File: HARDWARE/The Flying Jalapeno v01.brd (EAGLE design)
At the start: 73.7 x 52.1 mm, 79 parts, among them J1 ., J2 7V, Q1 8/16MHz, Q2 NPN, Q3 P-Channel MOSFET, Q4 NPN, Q5 P-Channel MOSFET, U1 ATMEGA328

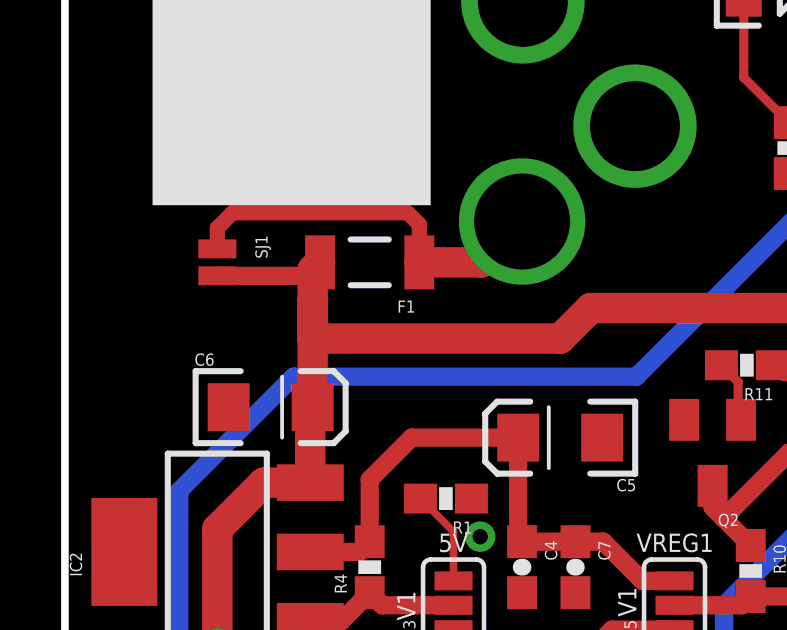
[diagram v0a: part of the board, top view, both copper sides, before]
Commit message: Power input Diode
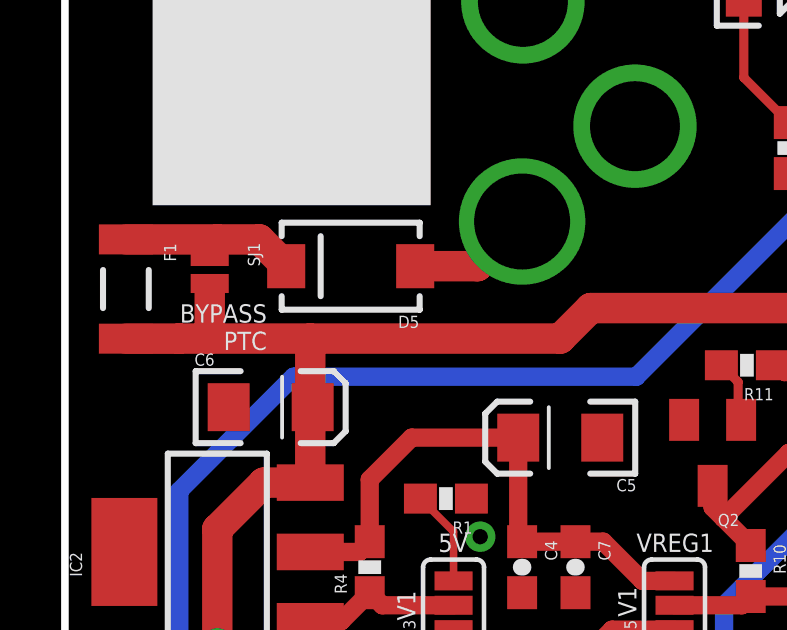
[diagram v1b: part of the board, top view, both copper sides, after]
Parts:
- added D5: MBRA140, SparkFun-DiscreteSemi:SMA-DIODE
- moved F1 8.18 mm to (2.03, 38.5), turned to 270 degrees
- moved SJ1 0.36 mm to (4.83, 39.1)
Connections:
- new net N$24: D5.A, J2.PWR
- net N$15: now also D5.C; no longer J2.PWR
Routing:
- net N$15: track 13.1 -> 6.39 mm
- net N$24: track 0.00 -> 4.18 mm
- net RAW: track 119.7 -> 120.6 mm
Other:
- board text added: "BYPASS PTC"
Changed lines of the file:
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@@
 <?xml version="1.0" encoding="utf-8"?>
 <!DOCTYPE eagle SYSTEM "eagle.dtd">
-<eagle version="6.5.0">
+<eagle version="7.2.0">
 <drawing>
 <settings>
@@
 <layer number="47" name="Measures" color="7" fill="1" visible="no" active="yes"/>
 <layer number="48" name="Document" color="7" fill="1" visible="no" active="yes"/>
-<layer number="49" name="Reference" color="13" fill="1" visible="yes" active="yes"/>
+<layer number="49" name="Reference" color="13" fill="1" visible="no" active="yes"/>
 <layer number="50" name="dxf" color="7" fill="1" visible="no" active="yes"/>
 <layer number="51" name="tDocu" color="6" fill="1" visible="yes" active="yes"/>
@@
 <text x="67.945" y="48.387" size="1.27" layer="21" font="vector" ratio="15">FTDI</text>
 <text x="66.675" y="47.117" size="1.016" layer="21" font="vector" ratio="15">VOLTAGE</text>
+<text x="6.731" y="37.973" size="0.6096" layer="21" font="vector" ratio="15" rot="R180">BYPASS
+ PTC</text>
 </plain>
 <attributes>
@@
 <pass name="Default">
 <param name="RoutingGrid" value="5mil"/>
+<param name="AutoGrid" value="1"/>
+<param name="Efforts" value="0"/>
+<param name="TopRouterVariant" value="1"/>
 <param name="tpViaShape" value="round"/>
 <param name="PrefDir.1" value="-"/>
@@
 <element name="C8" library="SparkFun-Capacitors" package="CPOL-RADIAL-100UF-25V" value="100uF" x="31.75" y="17.78" rot="MR270"/>
 <element name="FRAME1" library="SparkFun-Aesthetics" package="CREATIVE_COMMONS" value="FRAME-LEDGER" x="-1.27" y="-12.7"/>
-<element name="F1" library="Testing" package="PTC-1206-WIDE" value="" x="10.16" y="39.37" rot="R180"/>
+<element name="F1" library="Testing" package="PTC-1206-WIDE" value="" x="2.032" y="38.481" rot="R270"/>
 <element name="J2" library="SparkFun" package="POWER_JACK_PTH_LOCK" value="7V" x="15.24" y="54.61" rot="MR180"/>
-<element name="SJ1" library="SparkFun-Passives" package="PAD-JUMPER-2-NO_NO_SILK" value="PTC Bypass" x="5.08" y="39.37" rot="R270"/>
+<element name="SJ1" library="SparkFun-Passives" package="PAD-JUMPER-2-NO_NO_SILK" value="PTC Bypass" x="4.826" y="39.116" rot="R270"/>
 <element name="C9" library="SparkFun" package="0603-CAP" value="0.1uF" x="59.69" y="33.02" rot="R90"/>
 <element name="C10" library="SparkFun" package="EIA3216" value="10uF" x="43.18" y="46.99" rot="R180"/>
@@
 <element name="LOGO3" library="SparkFun-Aesthetics" package="SFE_LOGO_FLAME_.1" value="SFE_LOGO_FLAME.1_INCH" x="45.72" y="41.021"/>
 <element name="LOGO4" library="SparkFun-Aesthetics" package="OSHW-LOGO-L" value="OSHW-LOGOL" x="8.89" y="6.35" rot="MR0"/>
+<element name="D5" library="SparkFun-DiscreteSemi" package="SMA-DIODE" value="MBRA140" x="9.525" y="39.243" rot="R180">
+<attribute name="PROD_ID" value="DIO-08053" x="9.525" y="39.243" size="1.778" layer="27" font="vector" ratio="15" rot="R180" display="off"/>
+</element>
 </elements>
 <signals>
@@
 <contactref element="SJ6" pad="1"/>
 <contactref element="JP4" pad="4"/>
-<wire x1="8.506" y1="39.37" x2="8.258" y2="39.122" width="1.016" layer="1"/>
-<wire x1="8.258" y1="39.122" x2="8.258" y2="38.1" width="1.016" layer="1"/>
-<wire x1="8.258" y1="37.846" x2="8.258" y2="34.544" width="1.016" layer="1"/>
 <wire x1="8.258" y1="34.544" x2="8.1788" y2="34.4648" width="1.016" layer="1"/>
 <wire x1="8.1788" y1="34.4648" x2="8.1788" y2="32.0294" width="1.016" layer="1"/>
@@
 <wire x1="7.75" y1="22.225" x2="7.75" y2="19.8852" width="1.016" layer="1"/>
 <wire x1="7.75" y1="19.8852" x2="8.0518" y2="19.5834" width="1.016" layer="1"/>
-<wire x1="5.08" y1="38.92" x2="8.056" y2="38.92" width="0.6096" layer="1"/>
-<wire x1="8.056" y1="38.92" x2="8.506" y2="39.37" width="0.6096" layer="1"/>
 <wire x1="20.32" y1="27.1272" x2="18.2372" y2="27.1272" width="0.6096" layer="1"/>
 <wire x1="18.2372" y1="27.1272" x2="15.24" y2="24.13" width="0.6096" layer="1"/>
@@
 <wire x1="33.5788" y1="46.7614" x2="31.0134" y2="46.7614" width="1.016" layer="1"/>
 <wire x1="29.591" y1="45.339" x2="29.591" y2="40.132" width="1.016" layer="1"/>
-<wire x1="8.258" y1="37.846" x2="8.258" y2="38.1" width="1.016" layer="1"/>
 <wire x1="33.5788" y1="46.7614" x2="33.5788" y2="49.1012" width="1.016" layer="1"/>
 <wire x1="33.5788" y1="49.1012" x2="33.404" y2="49.276" width="1.016" layer="1"/>
@@
 <wire x1="17.78" y1="13.081" x2="17.78" y2="11.43" width="0.6096" layer="1"/>
 <via x="17.78" y="11.43" extent="1-16" drill="0.508"/>
-<wire x1="8.258" y1="37.846" x2="8.255" y2="36.83" width="1.016" layer="1"/>
-<wire x1="8.255" y1="36.83" x2="16.51" y2="36.83" width="1.016" layer="1"/>
 <wire x1="16.51" y1="36.83" x2="17.526" y2="37.846" width="1.016" layer="1"/>
 <wire x1="17.526" y1="37.846" x2="27.305" y2="37.846" width="1.016" layer="1"/>
 <wire x1="27.305" y1="37.846" x2="29.591" y2="40.132" width="1.016" layer="1"/>
 <wire x1="29.591" y1="45.339" x2="31.0134" y2="46.7614" width="1.016" layer="1"/>
+<wire x1="16.51" y1="36.83" x2="8.1788" y2="36.83" width="1.016" layer="1"/>
+<wire x1="8.1788" y1="36.83" x2="4.826" y2="36.83" width="1.016" layer="1"/>
+<wire x1="4.826" y1="36.83" x2="3.81" y2="36.83" width="1.016" layer="1"/>
+<wire x1="2.032" y1="36.827" x2="3.807" y2="36.827" width="1.016" layer="1"/>
+<wire x1="3.807" y1="36.827" x2="3.81" y2="36.83" width="1.016" layer="1"/>
+<wire x1="8.1788" y1="34.4648" x2="8.1788" y2="36.83" width="1.016" layer="1"/>
+<wire x1="4.826" y1="36.83" x2="4.826" y2="38.354" width="1.016" layer="1"/>
+<wire x1="4.826" y1="38.354" x2="4.826" y2="38.666" width="0.254" layer="1"/>
 </signal>
 <signal name="D9">
@@
 <signal name="N$15">
 <contactref element="F1" pad="1"/>
-<contactref element="J2" pad="PWR"/>
 <contactref element="SJ1" pad="1"/>
-<wire x1="15.24" y1="40.7322" x2="13.8778" y2="39.37" width="1.016" layer="1"/>
-<wire x1="13.8778" y1="39.37" x2="11.814" y2="39.37" width="1.016" layer="1"/>
-<wire x1="11.814" y1="39.37" x2="11.814" y2="40.637" width="0.508" layer="1"/>
-<wire x1="5.08" y1="39.82" x2="5.08" y2="40.513" width="0.508" layer="1"/>
-<wire x1="5.08" y1="40.513" x2="5.588" y2="41.021" width="0.508" layer="1"/>
-<wire x1="5.588" y1="41.021" x2="11.43" y2="41.021" width="0.508" layer="1"/>
-<wire x1="11.43" y1="41.021" x2="11.814" y2="40.637" width="0.508" layer="1"/>
+<contactref element="D5" pad="C"/>
+<wire x1="7.375" y1="39.243" x2="6.483" y2="40.135" width="1.016" layer="1"/>
+<wire x1="6.483" y1="40.135" x2="5.08" y2="40.135" width="1.016" layer="1"/>
+<wire x1="5.08" y1="40.135" x2="2.032" y2="40.135" width="1.016" layer="1"/>
+<wire x1="4.826" y1="39.566" x2="5.08" y2="39.82" width="0.254" layer="1"/>
+<wire x1="5.08" y1="39.82" x2="5.08" y2="40.135" width="0.254" layer="1"/>
 </signal>
 <signal name="N$3">
@@
 <wire x1="54.1061625" y1="20.32" x2="54.154421875" y2="20.368259375" width="0.254" layer="1"/>
 </signal>
+<signal name="N$24">
+<contactref element="J2" pad="PWR"/>
+<contactref element="D5" pad="A"/>
+<wire x1="15.24" y1="40.7322" x2="13.7508" y2="39.243" width="1.016" layer="1"/>
+<wire x1="13.7508" y1="39.243" x2="11.675" y2="39.243" width="1.016" layer="1"/>
+</signal>
 </signals>
 <errors>
@@
 </board>
 </drawing>
+<compatibility>
+<note version="6.3" minversion="6.2.2" severity="warning">
+Since Version 6.2.2 text objects can contain more than one line,
+which will not be processed correctly with this version.
+</note>
+</compatibility>
 </eagle>

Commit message: Some PROD_IDS and moved to 100uF SMD caps
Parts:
- C10, C11, C14, C15, C5, C6: device SparkFun:EIA3216 -> SparkFun-Capacitors:EIA3216
- C12, C13, C16, C17, C18, C4, C7, C9: device SparkFun:0603-CAP -> SparkFun-Capacitors:0603-CAP
- C3, C8: device SparkFun-Capacitors:CPOL-RADIAL-100UF-25V -> SparkFun-Capacitors:NIC_10X10.5_CAP
- J2: device SparkFun:POWER_JACK_PTH_LOCK -> SparkFun-Connectors:POWER_JACK_PTH_LOCK
- JP1: device SparkFun:1X06-SMD -> SparkFun-Connectors:1X06-SMD
- moved D4 8.15 mm to (31.1, 20.7), turned to 270 degrees
- moved D1 7.45 mm to (31.2, 26.3), turned to 270 degrees
- moved C8 6.48 mm to (38.1, 16.5), flipped to the top, turned to 180 degrees
- moved C3 6.35 mm to (38.1, 30.5), flipped to the top, turned to 180 degrees
- moved R9 6.21 mm to (46.0, 35.8)
- moved R3 5.33 mm to (46.0, 34.3)
- moved R5 4.91 mm to (31.5, 35.3)
- moved R29 4.88 mm to (44.5, 23.0), turned to 180 degrees
- moved R13 3.78 mm to (46.5, 30.6)
- moved R20 2.47 mm to (36.4, 23.0), turned to 0 degrees
- moved R28 1.42 mm to (40.9, 23.0)
- moved R30 1.27 mm to (44.7, 20.7)
- moved R23 0.90 mm to (40.0, 9.78), turned to 0 degrees
- moved R24 0.63 mm to (45.1, 10.4)
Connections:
- net GND: now also C3.-, C8.-; no longer C3.2, C8.2
- net N$22: now also C3.+; no longer C3.1
- net N$23: now also C8.+; no longer C8.1
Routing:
- net V1: track 47.6 -> 56.3 mm
- net N$5: track 3.69 -> 9.51 mm, vias 0 -> 2
- net A7/PRETESTREAD_V2: track 62.1 -> 65.7 mm
- net A6/PRETESTREAD_V1: track 53.7 -> 50.7 mm
- net N$22: track 12.2 -> 14.6 mm
- net V2: track 33.0 -> 35.2 mm
- net PT-FAIL: track 8.73 -> 6.84 mm
- net N$23: track 12.3 -> 14.2 mm
- net N$11: track 3.49 -> 4.81 mm
- net D5: track 37.4 -> 36.2 mm
- net D12/PRETEST-WRITE: track 81.8 -> 80.8 mm
- net RX: track 66.4 -> 65.4 mm
- net TX: track 58.0 -> 57.3 mm

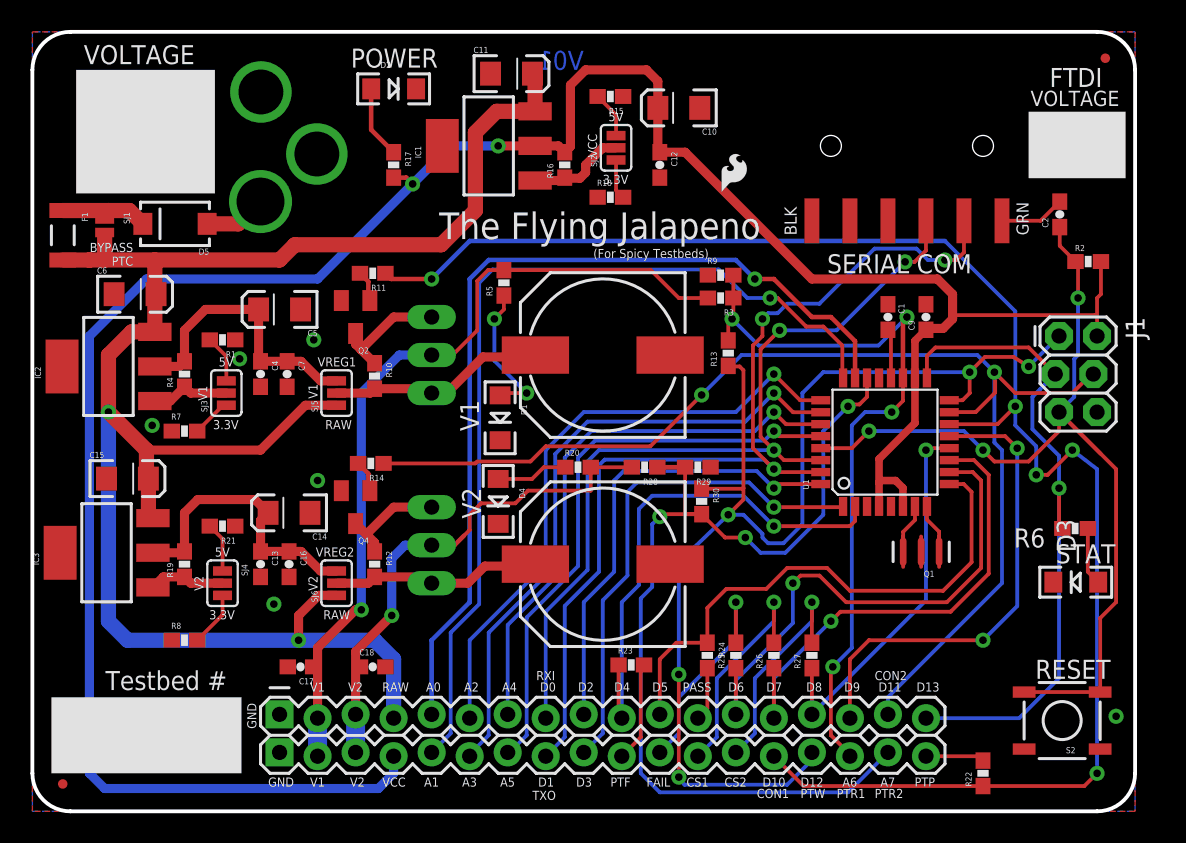
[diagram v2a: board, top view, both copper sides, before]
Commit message: more PROD_IDs
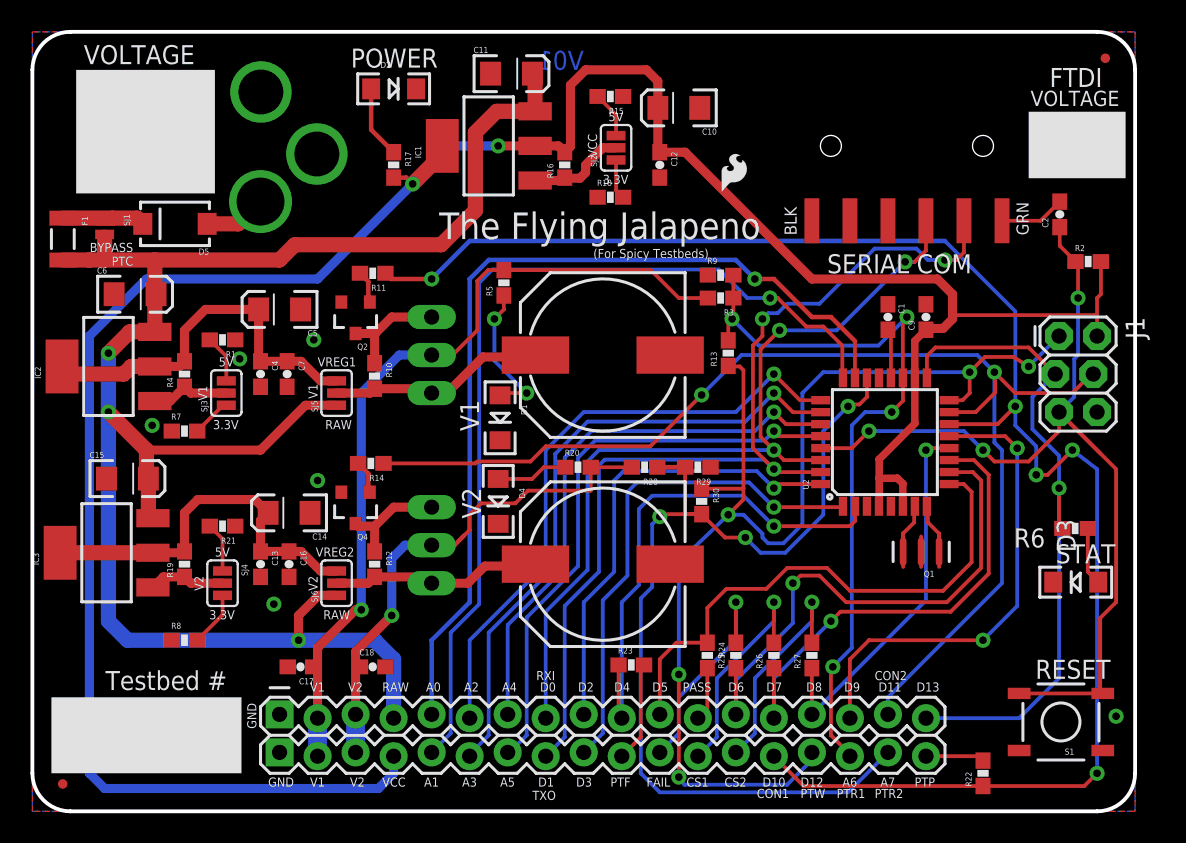
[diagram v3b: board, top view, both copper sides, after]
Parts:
- removed S2: Reset, SparkFun:TACTILE_SWITCH_SMD
- removed U1: ATMEGA328, SparkFun:TQFP32-08
- added S1: (no value), SparkFun-Electromechanical:TACTILE-SWITCH-SMD
- added U2: ATMEGA328P_TQFP, SparkFun-DigitalIC:TQFP32-08
- D1, D2, D3, D4: value Green -> RED
- F1: device Testing:PTC-1206-WIDE -> SparkFun-PowerIC:PTC-1206
- IC1, IC2, IC3: device SparkFun:SOT223 -> SparkFun-PowerIC:SOT223
- Q1: value 8/16MHz -> 16MHZ; device Testing:RESONATOR-SMD-1:1 -> SparkFun-FreqCtrl:RESONATOR-SMD
- Q2, Q4: value NPN -> MMBT2222A; device SparkFun:SOT23 -> SparkFun-DiscreteSemi:SOT23-3
- R1, R10, R11, R12, R14, R15, R16, R19, R4, R8: device SparkFun:0603-RES -> SparkFun-Resistors:0603-RES
- R13, R28, R3, R30: device Testing:0603-RES -> SparkFun-Resistors:0603-RES
- R17, R20, R22, R23, R24, R25, R5, R6: value 330 -> 390
- R26, R27: value 20M -> 22M ohm
- R29, R9: value 100K -> 100k; device Testing:0603-RES -> SparkFun-Resistors:0603-RES
- moved F1 0.25 mm to (2.03, 38.2)
- moved SJ1 0.13 mm to (4.83, 39.0)
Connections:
- removed net N$25: C13.1, C14.A, C16.1, IC3.2, R19.2, SJ6.3
- new net VREG2OUT: C13.1, C14.A, C16.1, IC3.2, IC3.4, R19.2, SJ6.3
- net A0: now also U2.23; no longer U1.23
- net A1: now also U2.24; no longer U1.24
- net A2: now also U2.25; no longer U1.25
- net A3: now also U2.26; no longer U1.26
- net A4: now also U2.27; no longer U1.27
- net A5: now also U2.28; no longer U1.28
- net A6/PRETESTREAD_V1: now also U2.19; no longer U1.19
- net A7/PRETESTREAD_V2: now also U2.22; no longer U1.22
- net AREF: now also U2.20; no longer U1.20
- net D10/CONT1: now also U2.14; no longer U1.14
- net D11/CONT2: now also U2.15; no longer U1.15
- net D12/PRETEST-WRITE: now also U2.16; no longer U1.16
- net D2: now also U2.32; no longer U1.32
- net D3: now also U2.1; no longer U1.1
- net D4: now also U2.2; no longer U1.2
- net D5: now also U2.9; no longer U1.9
- net D6: now also U2.10; no longer U1.10
- net D7: now also U2.11; no longer U1.11
- net D8: now also U2.12; no longer U1.12
- net D9: now also U2.13; no longer U1.13
- net GND: now also S1.1, S1.2, U2.21, U2.3, U2.5; no longer S2.1, S2.2, U1.21, U1.3, U1.5
- net N$1: now also U2.8; no longer U1.8
- net N$2: now also U2.7; no longer U1.7
- net N$21: now also IC2.4
- net RESET: now also S1.3, S1.4, U2.29; no longer S2.3, S2.4, U1.29
- net RX: now also U2.31; no longer U1.31
- net SCK: now also U2.17; no longer U1.17
- net TX: now also U2.30; no longer U1.30
- net VCC: now also IC1.4, U2.18, U2.4, U2.6; no longer U1.18, U1.4, U1.6
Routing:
- net VREG2OUT: track 0.00 -> 25.7 mm
- net N$25: track 19.5 -> 0.00 mm
- net N$21: track 18.9 -> 25.5 mm
- net VCC: track 164.4 -> 167.9 mm
- net RESET: track 62.5 -> 63.2 mm
- net N$12: track 8.13 -> 7.52 mm
- net RAW: vias 2 -> 3

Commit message: more prod ids
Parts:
- Q3, Q5: device Testing:TO220V -> SparkFun-DiscreteSemi:TO220V
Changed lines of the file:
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@@
 <attribute name="VALUE" value="100" x="22.733" y="35.941" size="1.778" layer="27" rot="R180" display="off"/>
 </element>
-<element name="Q3" library="Testing" package="TO220V" value="P-Channel MOSFET" x="26.67" y="30.48" rot="MR270"/>
+<element name="Q3" library="SparkFun-DiscreteSemi" package="TO220V" value="P-Channel MOSFET" x="26.67" y="30.48" rot="MR270">
+<attribute name="PROD_ID" value="TRANS-13060" x="26.67" y="30.48" size="1.778" layer="28" rot="MR270" display="off"/>
+</element>
 <element name="C3" library="SparkFun-Capacitors" package="NIC_10X10.5_CAP" value="100uF" x="38.1" y="30.48" rot="R180">
 <attribute name="PROD_ID" value="CAP-08362" x="38.1" y="30.48" size="1.778" layer="27" rot="R180" display="off"/>
@@
 <attribute name="VALUE" value="100" x="22.606" y="23.241" size="1.778" layer="27" rot="R180" display="off"/>
 </element>
-<element name="Q5" library="Testing" package="TO220V" value="P-Channel MOSFET" x="26.67" y="17.78" rot="MR270"/>
+<element name="Q5" library="SparkFun-DiscreteSemi" package="TO220V" value="P-Channel MOSFET" x="26.67" y="17.78" rot="MR270">
+<attribute name="PROD_ID" value="TRANS-13060" x="26.67" y="17.78" size="1.778" layer="28" rot="MR270" display="off"/>
+</element>
 <element name="C8" library="SparkFun-Capacitors" package="NIC_10X10.5_CAP" value="100uF" x="38.1" y="16.51" rot="R180">
 <attribute name="PROD_ID" value="CAP-08362" x="38.1" y="16.51" size="1.778" layer="27" rot="R180" display="off"/>
